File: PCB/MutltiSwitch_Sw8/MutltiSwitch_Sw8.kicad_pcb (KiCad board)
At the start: 2 copper layers, 38.7 x 32.4 mm, 24 parts, among them IC1 ATTINY84-P, IC2 ULN2803, P1 +V=VRx / +V<VRx, P10 OUTPUT_1X8_GND, P2 XANY_INPUT, P3 SERVO, P4 DIODE, P5 OUTPUT_1X8, P6 VExt, P7 OUTPUT_1X8_ALIM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

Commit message: Update_PCB_Multiswitch_8
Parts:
- added R10: 10K, R_1206, B.Cu at (156.8, 101.6)
- added R11: 10K, R_1206, B.Cu at (156.8, 104.1)
- added R12: 10K, R_1206, B.Cu at (156.8, 106.7)
- added R13: 10K, R_1206, B.Cu at (156.8, 109.2)
- added R6: 10K, R_1206, B.Cu at (156.8, 91.4)
- added R7: 10K, R_1206, B.Cu at (156.8, 94.0)
- added R8: 10K, R_1206, B.Cu at (156.7, 96.5)
- added R9: 10K, R_1206, B.Cu at (156.8, 99.1)
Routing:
- net +5V: track 53.3 -> 80.5 mm
- net Net-(IC2-Pad16): track 3.81 -> 6.30 mm
- net Net-(IC2-Pad17): track 3.81 -> 6.22 mm
- net Net-(IC2-Pad18): track 3.81 -> 6.17 mm
- net Net-(IC2-Pad15): track 3.81 -> 6.17 mm
- net Net-(IC2-Pad14): track 3.81 -> 6.17 mm
- net Net-(IC2-Pad13): track 3.81 -> 6.17 mm
- net Net-(IC2-Pad12): track 3.81 -> 6.17 mm
- net Net-(IC2-Pad11): track 3.81 -> 6.17 mm
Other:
- board text added: "8X10K"
- board text added: "VExt GND"

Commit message: Push of MS8 PCB folder for Pierrot :-)
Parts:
- R3: value 100 -> 1K
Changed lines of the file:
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@@
     (visible_elements 7FFD7DDF)
     (pcbplotparams
-      (layerselection 0x00030_7ffffffe)
+      (layerselection 0x10000_7ffffffe)
       (usegerberextensions false)
       (usegerberattributes false)
       (usegerberadvancedattributes false)
       (creategerberjobfile false)
-      (excludeedgelayer true)
+      (excludeedgelayer false)
       (linewidth 0.100000)
       (plotframeref false)
@@
       (padsonsilk false)
       (subtractmaskfromsilk false)
-      (outputformat 1)
-      (mirror false)
+      (outputformat 4)
+      (mirror true)
       (drillshape 0)
       (scaleselection 1)
@@
       (effects (font (size 1 1) (thickness 0.15)) (justify mirror))
     )
-    (fp_text value 100 (at 0 -1.95) (layer B.Fab)
-      (effects (font (size 1 1) (thickness 0.15)) (justify mirror))
-    )
+    (fp_text value 1K (at 0 -1.95) (layer B.Fab)
+      (effects (font (size 1 1) (thickness 0.15)) (justify mirror))
+    )

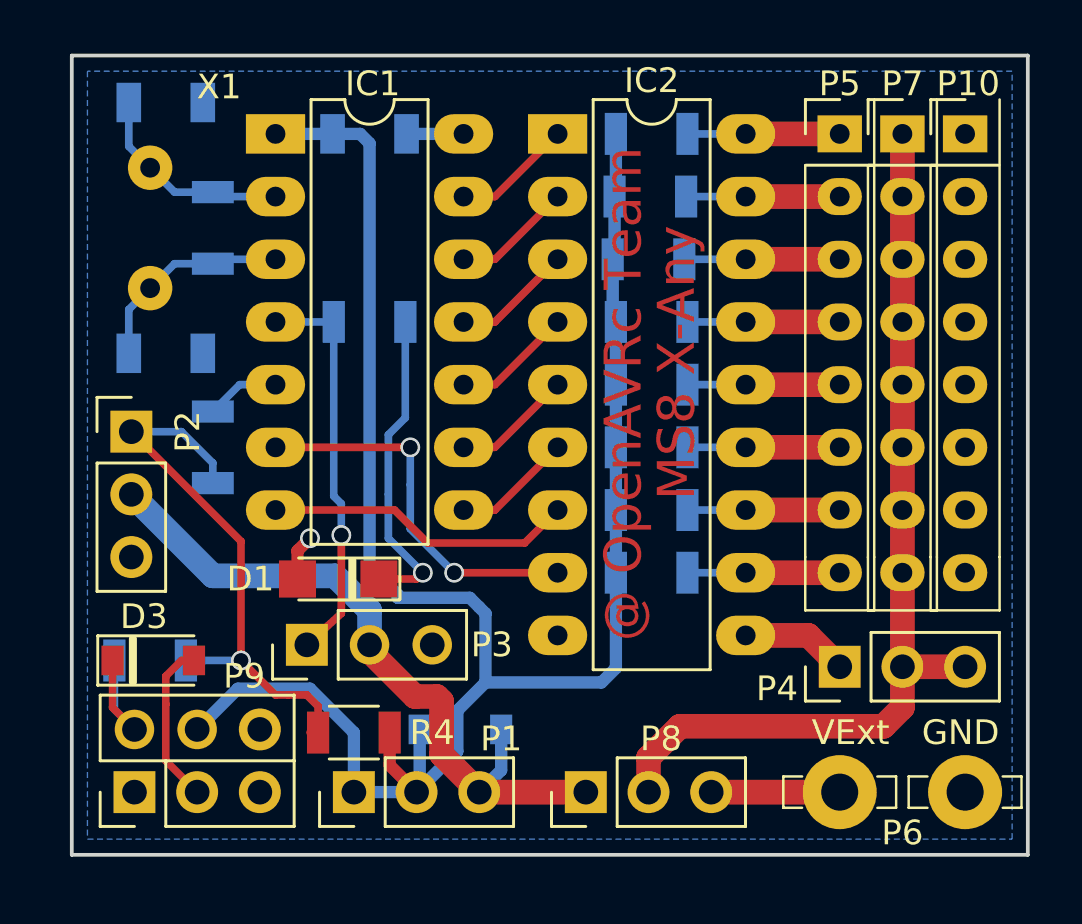
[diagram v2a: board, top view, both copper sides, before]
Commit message: MS8 Lost signal Led moved close to the Rx connector, doc updated accordingly
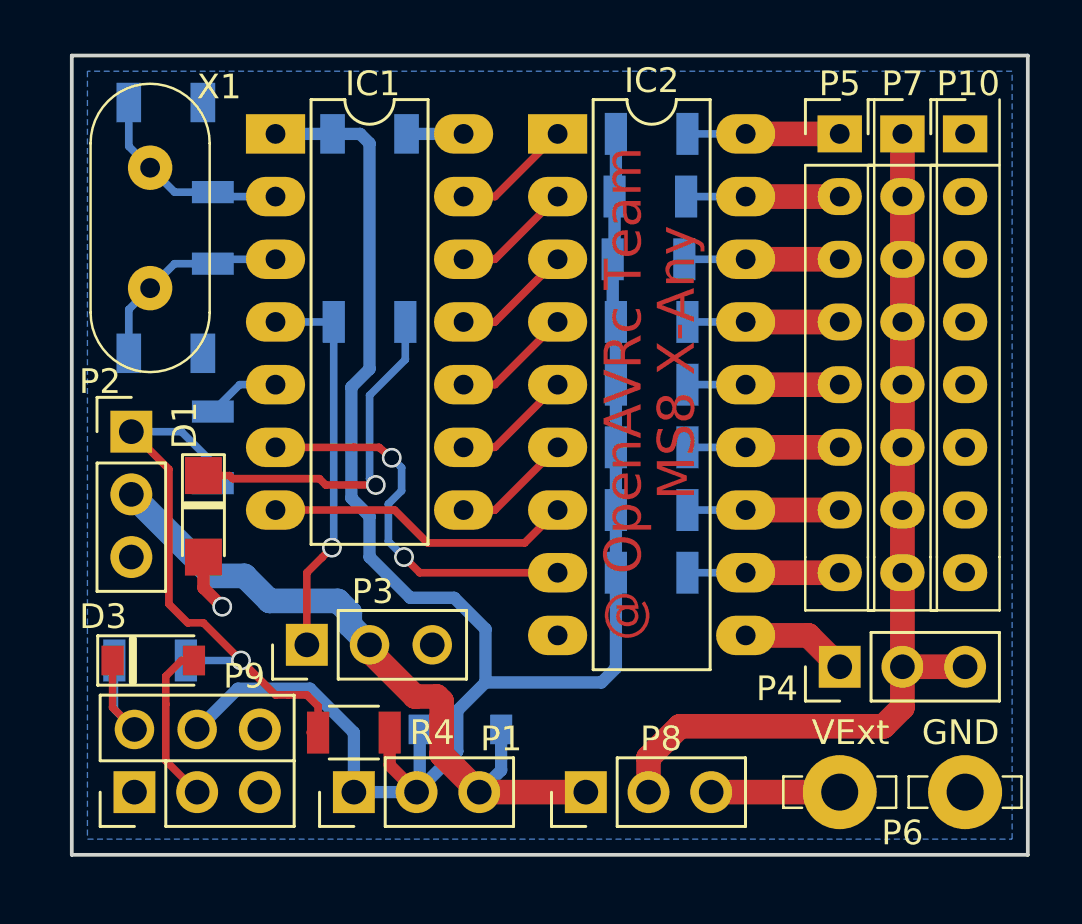
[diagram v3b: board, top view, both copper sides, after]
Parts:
- moved D1 6.02 mm to (138.7, 106.9), turned to 270 degrees
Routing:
- net Net-(D1-Pad1): track 13.2 -> 14.7 mm
- net Net-(IC1-Pad6): track 15.5 -> 16.1 mm
- net +VRx: track 28.6 -> 28.0 mm
